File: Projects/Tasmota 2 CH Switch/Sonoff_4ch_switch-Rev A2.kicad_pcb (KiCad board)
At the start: 2 copper layers, 99.8 x 99.1 mm, 64 parts, among them J1 Barrel_Jack_Switch, J2 Live, J3 Neutrals, J4 Earths, J5 Conn_01x03_Male, K1 G5LE-1, K2 G5LE-1, K3 G5LE-1, K4 G5LE-1, Q1 2N7002, Q2 2N7002, Q3 2N7002, Q4 2N7002, Q5 2N7002, Q6 2N7002, Q7 2N7002, Q8 2N7002, U1 AP1117-50, U2 Wemos_D1_Mini_wide

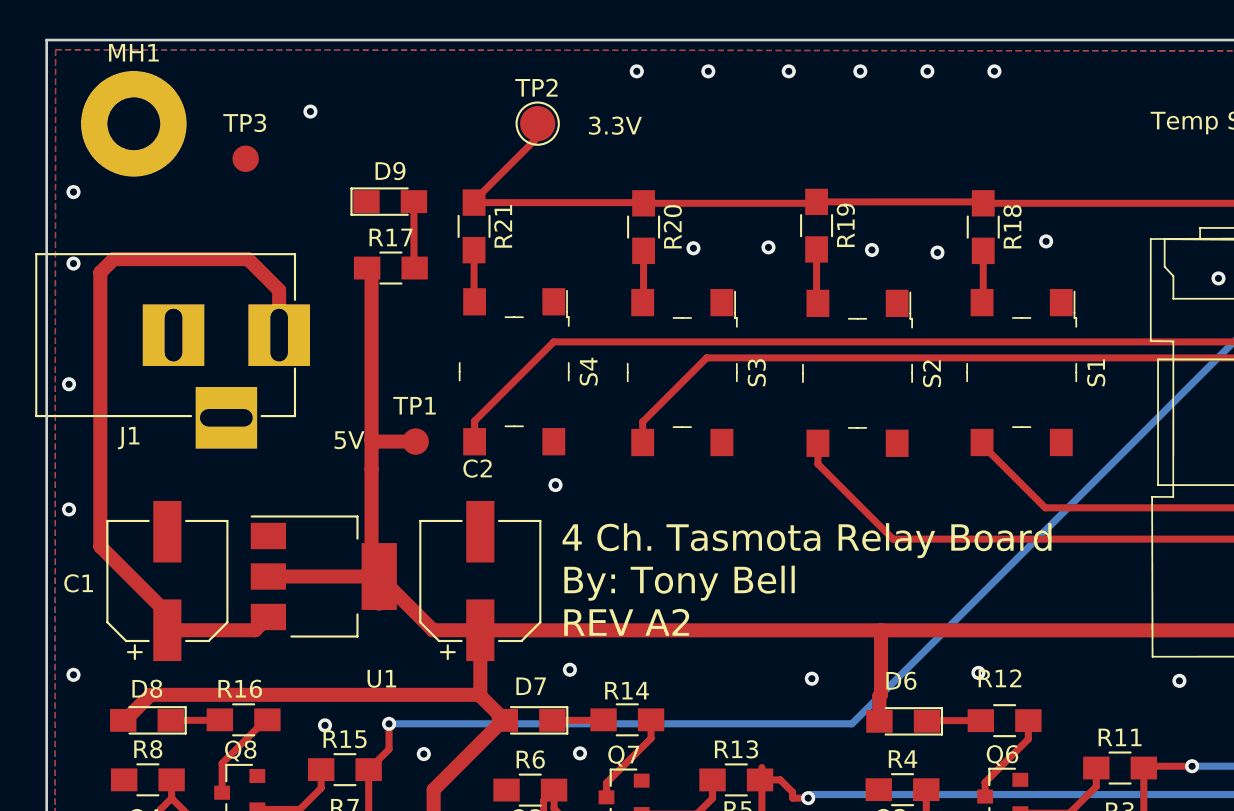
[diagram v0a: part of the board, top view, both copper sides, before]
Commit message: Created new 2Ch Tasmota Switch
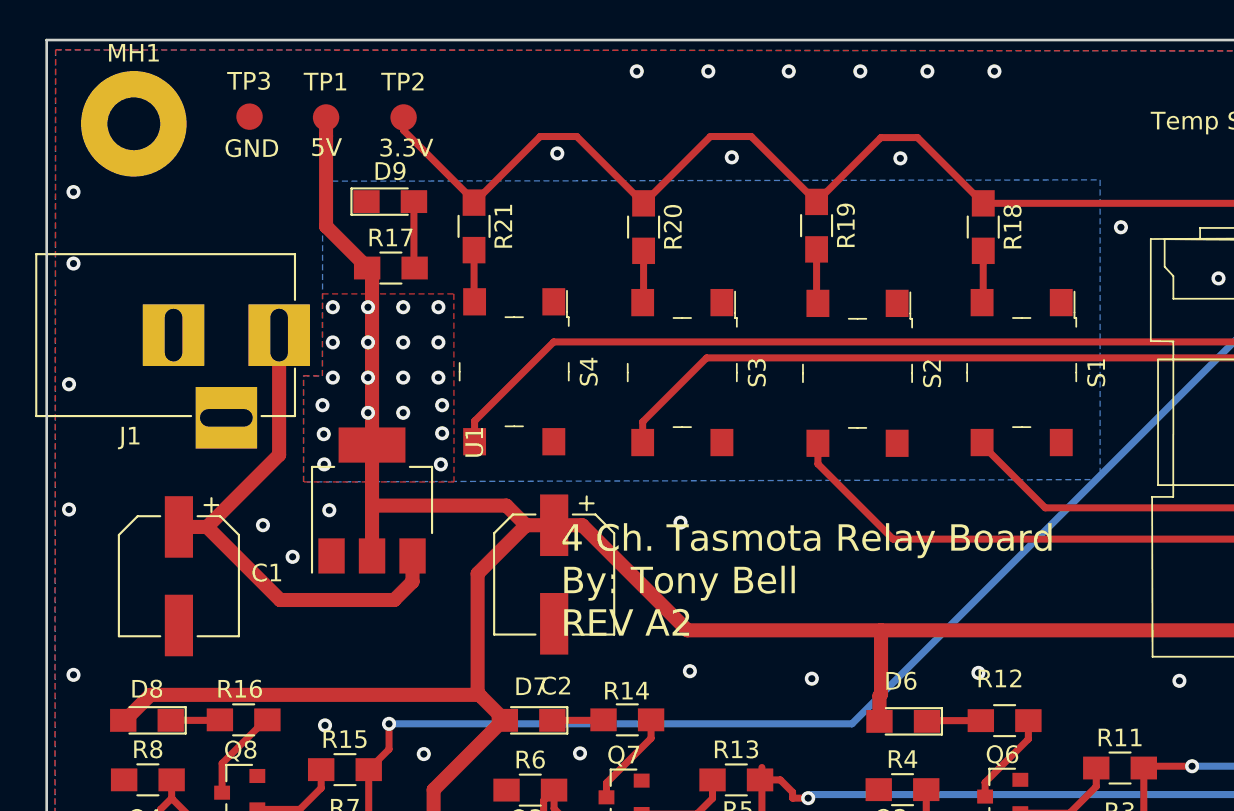
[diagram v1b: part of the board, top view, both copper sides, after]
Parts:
- TP2: footprint TestPoint:TestPoint_Pad_D2.0mm -> Measurement_Points:Measurement_Point_Round-SMD-Pad_Small
- moved TP1 19.1 mm to (96.9, 36.9)
- moved TP2 7.63 mm to (101.3, 36.9)
- moved U1 5.11 mm to (99.5, 58.7), turned to 90 degrees
- moved C2 4.21 mm to (109.9, 62.9), turned to 270 degrees
- moved TP3 2.40 mm to (92.6, 36.9)
- moved C1 0.71 mm to (88.5, 63.0), turned to 270 degrees
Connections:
- S1 pad 1: GND -> Net-(S1-Pad1)
- S2 pad 1: GND -> Net-(S2-Pad1)
- S3 pad 1: GND -> Net-(S3-Pad1)
- S4 pad 1: GND -> Net-(S4-Pad1)
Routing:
- net /DC_IN: track 41.7 -> 29.5 mm
- net +3V3: track 61.7 -> 71.5 mm
- net +5V: track 262.9 -> 269.6 mm, vias 4 -> 24
- net GND: vias 70 -> 71
- added copper zone on B.Cu, net +5V
- added copper zone on F.Cu, net +5V
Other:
- board text added: "GND"
